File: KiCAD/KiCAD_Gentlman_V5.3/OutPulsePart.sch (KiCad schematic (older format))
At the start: 0 parts

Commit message: KSG : V5.3 회로도 초본 완성(검토 필요) 일부 부품 데이터시트 추가
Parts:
- added C17, C19, C24, C25, C26, C27, C28, C29, C31, C32, C36, C37, C39, C40: CAP_101K_250V_2012, symbol Custom:CAP_101K_250V_2012
- added C18, C30, C41, C46: CAP_220uF_6.3V_SC6.3X5.8, symbol Custom:CAP_220uF_6.3V_SC6.3X5.8
- added C20, C33, C42, C47: CAP_103K_250V_3216, symbol Custom:CAP_103K_250V_3216
- added C21, C22, C34, C35, C43, C44, C48, C49: CAP_105K_250V_4532, symbol Custom:CAP_105K_250V_4532
- added C23, C38, C45, C50, C?: CAP_103K_25V_1608, symbol Custom:CAP_103K_25V_1608
- added CN5: 12505WS-09(STRAIGHT), symbol Custom:Conn_01x09
- added CN6: 12505WS-08(STRAIGHT), symbol Custom:Conn_01x08
- added D11, D8, D9, D?: MBRAF3200T3G, Diode_SMD:D_SMA, symbol Custom:MBRAF3200T3G
- added FET1, FET2, FET3, FET4: FDT86246L, symbol Custom:FDT86246L
- added L1, L2, L3, L4: SC7850D-221K, symbol Custom:SC7850D-221K
- added Q10, Q11, Q12, Q15, Q16, Q17, Q18, Q23, Q24, Q25, Q26, Q27, Q28, Q29, Q30, Q9, Q? (x8): 2N5551S, symbol Custom:2N5551S
- added Q13, Q14, Q19, Q20, Q21, Q22, Q7, Q8, Q? (x4): 2N5401S, Package_TO_SOT_SMD:TSOT-23, symbol Custom:2N5401S
- added R100, R103, R106, R119, R120, R121, R122, R127, R130, R133, R136, R41, R42, R47, R50, R66, R67, R73, R76, R89, R90, R91, R92, R97, R?: R_1KF, symbol Custom:R_1KF
- added R101, R102, R104, R105, R107, R110, R111, R112, R113, R115, R116, R117, R118, R124, R126, R128, R129, R131, R132, R134, R135, R137, R32, R33, R39, R40, R44, R46, R48, R49, R51, R54, R55, R60, R70, R72, R74, R75, R77, R80, R81, R82, R83, R85, R86, R87, R88, R94, R96, R98, R99, R?: R_100KJ, symbol Custom:R_100KJ
- added R108, R114, R30, R38, R52, R59, R78, R84: R_150KF_2012, symbol Custom:R_150KF_2012
- added R109, R31, R53, R79: R_120RJ_3216, symbol Custom:R_120RJ_3216
- added R123, R43, R69, R93: R_100RJ, symbol Custom:R_100RJ
- added R125, R45, R71, R95: R_8.2KF, symbol Custom:R_8.2KF
- added R34, R35, R36, R37, R? (x8): R_2.7KF, symbol Custom:R_2.7KF
- added R?: R_0RJ_6432, symbol Custom:R_0RJ_6432
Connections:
- net labels added: +5V, CH1_OP1, CH1_OP2, CH1_P1_CTL1, CH1_P1_CTL2, CH1_P2_CTL1, CH1_P2_CTL2, CH2_OP1, CH2_OP2, CH2_P1_CTL1, CH2_P1_CTL2, CH2_P2_CTL1, CH2_P2_CTL2, CH3_OP1, CH3_OP2, CH3_OP3, CH3_OP4, CH3_P1_CTL1, CH3_P1_CTL2, CH3_P2_CTL1, CH3_P2_CTL2, CH3_P3_CTL1, CH3_P3_CTL2, CH3_P4_CTL1, CH3_P4_CTL2, CH4_OP1, CH4_OP2, CH4_OP3, CH4_OP4, CH4_P1_CTL1, CH4_P1_CTL2, CH4_P2_CTL1, CH4_P2_CTL2, CH4_P3_CTL1, CH4_P3_CTL2, CH4_P4_CTL1, CH4_P4_CTL2, CTL_CH1, CTL_CH2, CTL_CH3, CTL_CH4, GNDPWR, GNDREF, H_CURR_CH, H_VOLT_CH1, H_VOLT_CH2, H_VOLT_CH3, H_VOLT_CH4, N.C, RGB_B6, RGB_COM6, RGB_G6, RGB_R6
- wire segments 0 -> 533

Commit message: KSG : V5.3 회로도 완성, 심볼 정보 업데이트 완료(데이터시트 및 풋프린트 등), 기존 BOM과 일치 완료
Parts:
- C17, C19, C24, C25, C26, C27, C28, C29, C31, C32, C36, C37, C39, C40: footprint (none) -> Custom:C_0805_2012Metric; Comment (none) -> 101K/250V; Description (none) -> CHIP CERAMIC CAP; MAKER (none) -> WALSIN, SAMSUNG; TYPE (none) -> 2012
- C18, C30, C41, C46: footprint (none) -> Custom:C_Elec_6.3x5.8; Comment (none) -> 220uF/6.3V; Description (none) -> SMD ELECT CAPACITOR; Field4 (none) -> 220uF/6.3V; MAKER (none) -> SAMYOUNG; TYPE (none) -> SC 6.3X5.8; ValueView 220uF/6.3V -> (none)
- C20, C33, C42, C47: footprint (none) -> Custom:C_1206_3216Metric; Comment (none) -> TCC1206X7R103K251DT; Description (none) -> CHIP CERAMIC CAP; MAKER (none) -> CCTC; TYPE (none) -> 3216
- C21, C22, C34, C35, C43, C44, C48, C49: footprint (none) -> Custom:C_1812_4532Metric; Comment (none) -> FS43X105K251EGG; Description (none) -> CHIP CERAMIC CAP; MAKER (none) -> WALSIN; TYPE (none) -> 4532
- C23, C38, C45, C50: footprint (none) -> Custom:C_0603_1608Metric; Comment (none) -> 103K/25V; Description (none) -> CHIP CERAMIC CAP; MAKER (none) -> WALSIN, SAMSUNG; TYPE (none) -> 1608
- C51: renamed from C?; footprint (none) -> Custom:C_0603_1608Metric; Comment (none) -> 103K/25V; Description (none) -> CHIP CERAMIC CAP; MAKER (none) -> WALSIN, SAMSUNG; TYPE (none) -> 1608
- CN5: value 12505WS-09(STRAIGHT) -> 12505WS-09; footprint (none) -> Custom:12505WS-09; symbol Custom:Conn_01x09 -> Custom:12505WS-09; Comment (none) -> 12505WS-09; Description (none) -> SMD WAFER; MAKER (none) -> YEONHO ELECTRONICS; TYPE (none) -> SMD-9
- CN6: value 12505WS-08(STRAIGHT) -> 12505WS-08; footprint (none) -> Custom:12505WS-08; symbol Custom:Conn_01x08 -> Custom:12505WS-08; Comment (none) -> 12505WS-08; Description (none) -> SMD WAFER; MAKER (none) -> YEONHO ELECTRONICS; TYPE (none) -> SMD-8
- D10: renamed from D?; footprint Diode_SMD:D_SMA -> Custom:D_SMA; Comment (none) -> MBRAF3200T3G; Description (none) -> SMD DIODE SCHOTTKY; MAKER (none) -> MDD, ON SEMICONDUCTOR; TYPE (none) -> SMA
- D11, D8, D9: footprint Diode_SMD:D_SMA -> Custom:D_SMA; Comment (none) -> MBRAF3200T3G; Description (none) -> SMD DIODE SCHOTTKY; MAKER (none) -> MDD, ON SEMICONDUCTOR; TYPE (none) -> SMA
- FET1, FET2, FET3, FET4: footprint (none) -> Custom:SOT-223-3_TabPin2; Comment (none) -> FDT86246L; Description (none) -> SMD MOSFET N-CHANNEL; MAKER (none) -> FAIRCHILD; TYPE (none) -> SOT-223
- L1, L2, L3, L4: footprint (none) -> Custom:L_SC7850D-221K; Comment (none) -> SC7850D-221K; Description (none) -> SMD INDUCTOR; MAKER (none) -> SUHKWANG; TYPE (none) -> 7850
- Q10, Q11, Q12, Q15, Q16, Q17, Q18, Q23, Q24, Q25, Q26, Q27, Q28, Q29, Q30, Q9: footprint (none) -> Custom:SOT-23; Comment (none) -> 2N5551S; Description (none) -> CHIP TRANSISTOR; MAKER (none) -> FIRST SILICON; TYPE (none) -> SOT-23
- Q13, Q14, Q19, Q20, Q21, Q22, Q7, Q8: footprint Package_TO_SOT_SMD:TSOT-23 -> Custom:SOT-23; Comment (none) -> 2N5401S; Description (none) -> CHIP TRANSISTOR; MAKER (none) -> FIRST SILICON; TYPE (none) -> SOT-23
- Q31, Q32, Q33, Q34: renamed from Q?; footprint Package_TO_SOT_SMD:TSOT-23 -> Custom:SOT-23; Comment (none) -> 2N5401S; Description (none) -> CHIP TRANSISTOR; MAKER (none) -> FIRST SILICON; TYPE (none) -> SOT-23
- Q35, Q36, Q37, Q38, Q39, Q40, Q41, Q42: renamed from Q?; footprint (none) -> Custom:SOT-23; Comment (none) -> 2N5551S; Description (none) -> CHIP TRANSISTOR; MAKER (none) -> FIRST SILICON; TYPE (none) -> SOT-23
- R100, R103, R106, R119, R120, R121, R122, R127, R130, R133, R136, R41, R42, R47, R50, R66, R67, R73, R76, R89, R90, R91, R92, R97: footprint (none) -> Custom:R_0603_1608Metric; Comment (none) -> 1KF; Description (none) -> CHIP RESISTOR; MAKER (none) -> WALSIN, SAMSUNG; TYPE (none) -> 1608
- R101, R102, R104, R105, R107, R110, R111, R112, R113, R115, R116, R117, R118, R124, R126, R128, R129, R131, R132, R134, R135, R137, R32, R33, R39, R40, R44, R46, R48, R49, R51, R54, R55, R60, R70, R72, R74, R75, R77, R80, R81, R82, R83, R85, R86, R87, R88, R94, R96, R98, R99: footprint (none) -> Custom:R_0603_1608Metric; Comment (none) -> 100KJ; Description (none) -> CHIP RESISTOR; MAKER (none) -> WALSIN, SAMSUNG; TYPE (none) -> 1608
- R108, R114, R30, R38, R52, R59, R78, R84: footprint (none) -> Custom:R_0805_2012Metric; Comment (none) -> 150KF; Description (none) -> CHIP RESISTOR; MAKER (none) -> WALSIN, SAMSUNG; TYPE (none) -> 2012
- R109, R31, R53, R79: footprint (none) -> Custom:R_1206_3216Metric; Comment (none) -> 120RJ; Description (none) -> CHIP RESISTOR; MAKER (none) -> WALSIN, SAMSUNG; TYPE (none) -> 3216
- R123, R43, R69, R93: footprint (none) -> Custom:R_0603_1608Metric; Comment (none) -> 100RJ; Description (none) -> CHIP RESISTOR; MAKER (none) -> WALSIN, SAMSUNG; TYPE (none) -> 1608
- R125, R45, R71, R95: footprint (none) -> Custom:R_0603_1608Metric; Comment (none) -> 8.2KF; Description (none) -> CHIP RESISTOR; MAKER (none) -> WALSIN, SAMSUNG; TYPE (none) -> 1608
- R138: renamed from R?; footprint (none) -> Custom:R_3522_6432Metric; Comment (none) -> 0RJ; Description (none) -> CHIP RESISTOR; MAKER (none) -> WALSIN, SAMSUNG; TYPE (none) -> 6432
- R139: renamed from R?; footprint (none) -> Custom:R_0603_1608Metric; Comment (none) -> 1KF; Description (none) -> CHIP RESISTOR; MAKER (none) -> WALSIN, SAMSUNG; TYPE (none) -> 1608
- R34, R35, R36, R37: footprint (none) -> Custom:R_0603_1608Metric; Comment (none) -> 2.7KF; Description (none) -> CHIP RESISTOR; MAKER (none) -> WALSIN, SAMSUNG; TYPE (none) -> 1608
- R56, R57, R58, R62, R63, R64, R65, R68: renamed from R?; footprint (none) -> Custom:R_0603_1608Metric; Comment (none) -> 2.7KF; Description (none) -> CHIP RESISTOR; MAKER (none) -> WALSIN, SAMSUNG; TYPE (none) -> 1608
- R61: renamed from R?; footprint (none) -> Custom:R_0603_1608Metric; Comment (none) -> 100KJ; Description (none) -> CHIP RESISTOR; Field4 61 -> 100KJ; MAKER (none) -> WALSIN, SAMSUNG; TYPE (none) -> 1608

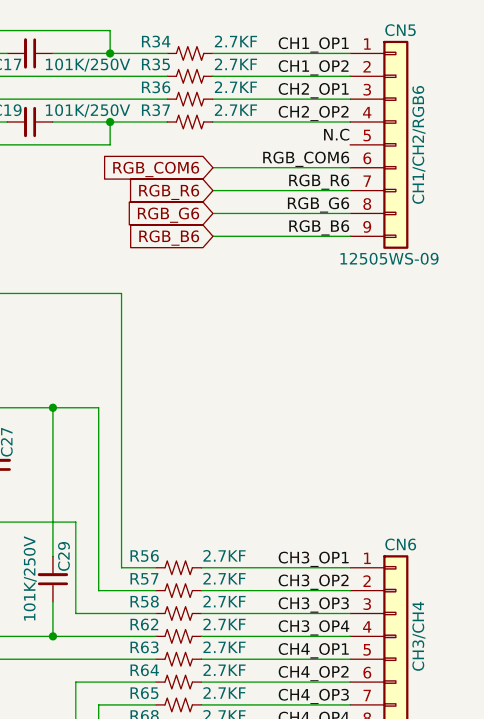
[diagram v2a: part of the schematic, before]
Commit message: KSG : 블루투스 회로도 작성 완료 (풋프린트 및 데이터시트 업데이트 완료)
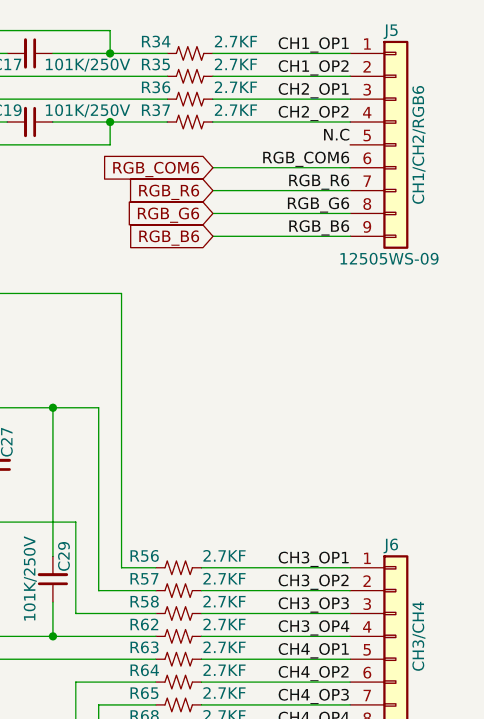
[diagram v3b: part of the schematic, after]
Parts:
- renumbered CN5 to J5, CN6 to J6
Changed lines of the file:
@@
 $Descr A3 16535 11693
 encoding utf-8
-Sheet 3 3
+Sheet 3 4
 Title "GentlemanV5.3"
 Date "2021-10-19"
@@
 Connection ~ 3350 7200
 $Comp
-L Custom:12505WS-09 CN5
+L Custom:12505WS-09 J5
 U 1 1 61F33BCC
 P 15450 1200
-F 0 "CN5" H 15400 1700 50  0000 L CNN
+F 0 "J5" H 15400 1700 50  0000 L CNN
 F 1 "12505WS-09" H 15200 700 50  0000 L CNN
 F 2 "Custom:12505WS-09" H 15450 1200 50  0001 C CNN
@@
 $EndComp
 $Comp
-L Custom:12505WS-08 CN6
+L Custom:12505WS-08 J6
 U 1 1 61F314D1
 P 15450 3350
-F 0 "CN6" H 15400 3750 50  0000 L CNN
+F 0 "J6" H 15400 3750 50  0000 L CNN
 F 1 "12505WS-08" H 15200 2850 50  0000 L CNN
 F 2 "Custom:12505WS-08" H 15450 3350 50  0001 C CNN

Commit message: KSG : V5.3B용으로 회로도 수정 및 PCB 아트웤 완료.(샘플PCB주문됨)
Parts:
- C17, C19, C24, C25, C26, C27, C28, C29, C31, C32, C36, C37, C39, C40: Comment 101K/250V -> (none); Description CHIP CERAMIC CAP -> (none); Field4 101K/250V -> (none); MAKER WALSIN, SAMSUNG -> (none); Maker (none) -> WALSIN, SAMSUNG; PartName (none) -> 101K/250V; Replacement (none) -> CC0805JRNPOYBN101; Shop (none) -> https://www.eleparts.co.kr/goods/view?no=9594793; TYPE 2012 -> (none); Type (none) -> CHIP CERAMIC CAP
- C18, C30, C41, C46: Comment 220uF/6.3V -> (none); Description SMD ELECT CAPACITOR -> (none); Field4 220uF/6.3V -> (none); Field5 SC 6.3X5.8 -> (none); MAKER SAMYOUNG -> (none); Maker (none) -> SAMYOUNG; PartName (none) -> 220uF/6.3V; Shop (none) -> https://www.eleparts.co.kr/goods/view?no=3369557; TYPE SC 6.3X5.8 -> (none); Type (none) -> SMD ELECT CAPACITOR
- C20, C33, C42, C47: Comment TCC1206X7R103K251DT -> (none); Description CHIP CERAMIC CAP -> (none); Field4 TCC1206X7R103K251DT -> (none); MAKER CCTC -> (none); Maker (none) -> CCTC; PartName (none) -> TCC1206X7R103K251DT; Shop (none) -> https://www.eleparts.co.kr/goods/view?no=8016042; TYPE 3216 -> (none); Type (none) -> CHIP CERAMIC CAP
- C21, C22, C34, C35, C43, C44, C48, C49: Comment FS43X105K251EGG -> (none); Description CHIP CERAMIC CAP -> (none); Field4 FS43X105K251EGG -> (none); MAKER WALSIN -> (none); Maker (none) -> WALSIN; PartName (none) -> FS43X105K251EGG; Shop (none) -> https://www.eleparts.co.kr/goods/view?no=8016951; TYPE 4532 -> (none); Type (none) -> CHIP CERAMIC CAP
- C23, C38, C45, C50, C51: Comment 103K/25V -> (none); Description CHIP CERAMIC CAP -> (none); Field4 103K/25V -> (none); MAKER WALSIN, SAMSUNG -> (none); Maker (none) -> WALSIN, SAMSUNG; PartName (none) -> 103K/25V; Replacement (none) -> CC0603KRX7R8BB103; Shop (none) -> https://www.eleparts.co.kr/goods/view?no=8057789#goodConten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; TYPE 1608 -> (none); Type (none) -> CHIP CERAMIC CAP
- D10, D11, D8, D9: Comment MBRAF3200T3G -> (none); Description SMD DIODE SCHOTTKY -> (none); MAKER MDD, ON SEMICONDUCTOR -> (none); Maker (none) -> MDD, ON SEMICONDUCTOR; PartName (none) -> MBRAF3200T3G; Replacement (none) -> SS1200-LTP; Shop (none) -> https://www.eleparts.co.kr/goods/view?no=1799117; TYPE SMA -> (none); Type (none) -> SMD DIODE SCHOTTKY
- FET1, FET2, FET3, FET4: Comment FDT86246L -> (none); Description SMD MOSFET N-CHANNEL -> (none); MAKER FAIRCHILD -> (none); Maker (none) -> FAIRCHILD; PartName (none) -> FDT86246L; Shop (none) -> https://www.eleparts.co.kr/goods/view?no=6008399; TYPE SOT-223 -> (none); Type (none) -> SMD MOSFET N-CHANNEL
- J5: Comment 12505WS-09 -> (none); Description SMD WAFER -> (none); Field4 CH1/CH2/RGB6 -> (none); MAKER YEONHO ELECTRONICS -> (none); Maker (none) -> YEONHO ELECTRONICS; PartName (none) -> 12505WS-09; Shop (none) -> https://www.devicemart.co.kr/goods/view?no=12012614; TYPE SMD-9 -> (none); Type (none) -> SMD WAFER
- J6: Comment 12505WS-08 -> (none); Description SMD WAFER -> (none); Field4 CH3/CH4 -> (none); MAKER YEONHO ELECTRONICS -> (none); Maker (none) -> YEONHO ELECTRONICS; PartName (none) -> 12505WS-08; Shop (none) -> https://www.devicemart.co.kr/goods/view?no=12012611; TYPE SMD-8 -> (none); Type (none) -> SMD WAFER
- L1, L2, L3, L4: Comment SC7850D-221K -> (none); Description SMD INDUCTOR -> (none); MAKER SUHKWANG -> (none); Maker (none) -> SUHKWANG; PartName (none) -> SC7850D-221K; Shop (none) -> https://www.devicemart.co.kr/goods/view?no=6606; TYPE 7850 -> (none); Type (none) -> SMD INDUCTOR
- Q10, Q11, Q12, Q15, Q16, Q17, Q18, Q23, Q24, Q25, Q26, Q27, Q28, Q29, Q30, Q35, Q36, Q37, Q38, Q39, Q40, Q41, Q42, Q9: Comment 2N5551S -> (none); Description CHIP TRANSISTOR -> (none); MAKER FIRST SILICON -> (none); Maker (none) -> FIRST SILICON; PartName (none) -> 2N5551S; Replacement (none) -> 2N5551S-RTK/P; Shop (none) -> KEC Semicon; TYPE SOT-23 -> (none); Type (none) -> CHIP TRANSISTOR
- Q13, Q14, Q19, Q20, Q21, Q22, Q31, Q32, Q33, Q34, Q7, Q8: Comment 2N5401S -> (none); Description CHIP TRANSISTOR -> (none); MAKER FIRST SILICON -> (none); Maker (none) -> FIRST SILICON; PartName (none) -> 2N5401S; Replacement (none) -> 2N5401S-RTK/P; Shop (none) -> https://www.eleparts.co.kr/goods/view?no=6561296; TYPE SOT-23 -> (none); Type (none) -> CHIP TRANSISTOR
- R100, R103, R106, R119, R120, R121, R122, R127, R130, R133, R136, R139, R41, R42, R47, R50, R66, R67, R73, R76, R89, R90, R91, R92, R97: Comment 1KF -> (none); Description CHIP RESISTOR -> (none); Field4 1KF -> (none); MAKER WALSIN, SAMSUNG -> (none); Maker (none) -> WALSIN, SAMSUNG; PartName (none) -> 1KF; TYPE 1608 -> (none); Type (none) -> CHIP RESISTOR
- R101, R102, R104, R105, R107, R110, R111, R112, R113, R115, R116, R117, R118, R124, R126, R128, R129, R131, R132, R134, R135, R137, R32, R33, R39, R40, R44, R46, R48, R49, R51, R54, R55, R60, R61, R70, R72, R74, R75, R77, R80, R81, R82, R83, R85, R86, R87, R88, R94, R96, R98, R99: Comment 100KJ -> (none); Description CHIP RESISTOR -> (none); Field4 100KJ -> (none); MAKER WALSIN, SAMSUNG -> (none); Maker (none) -> WALSIN, SAMSUNG; PartName (none) -> 100KJ; TYPE 1608 -> (none); Type (none) -> CHIP RESISTOR
- R108, R114, R30, R38, R52, R59, R78, R84: Comment 150KF -> (none); Description CHIP RESISTOR -> (none); Field4 150KF -> (none); MAKER WALSIN, SAMSUNG -> (none); Maker (none) -> WALSIN, SAMSUNG; PartName (none) -> 150KF; TYPE 2012 -> (none); Type (none) -> CHIP RESISTOR
- R109, R31, R53, R79: Comment 120RJ -> (none); Description CHIP RESISTOR -> (none); Field4 120RJ -> (none); MAKER WALSIN, SAMSUNG -> (none); Maker (none) -> WALSIN, SAMSUNG; PartName (none) -> 120RJ; TYPE 3216 -> (none); Type (none) -> CHIP RESISTOR
- R123, R43, R69, R93: Comment 100RJ -> (none); Description CHIP RESISTOR -> (none); Field4 100RJ -> (none); MAKER WALSIN, SAMSUNG -> (none); Maker (none) -> WALSIN, SAMSUNG; PartName (none) -> 100RJ; TYPE 1608 -> (none); Type (none) -> CHIP RESISTOR
- R125, R45, R71, R95: Comment 8.2KF -> (none); Description CHIP RESISTOR -> (none); Field4 8.2KF -> (none); MAKER WALSIN, SAMSUNG -> (none); Maker (none) -> WALSIN, SAMSUNG; PartName (none) -> 8.2KF; TYPE 1608 -> (none); Type (none) -> CHIP RESISTOR
- R138: Comment 0RJ -> (none); Description CHIP RESISTOR -> (none); Field4 0RJ -> (none); MAKER WALSIN, SAMSUNG -> (none); Maker (none) -> WALSIN, SAMSUNG; PartName (none) -> 0RJ; TYPE 6432 -> (none); Type (none) -> CHIP RESISTOR
- R34, R35, R36, R37, R56, R57, R58, R62, R63, R64, R65, R68: Comment 2.7KF -> (none); Description CHIP RESISTOR -> (none); Field4 2.7KF -> (none); MAKER WALSIN, SAMSUNG -> (none); Maker (none) -> WALSIN, SAMSUNG; PartName (none) -> 2.7KF; TYPE 1608 -> (none); Type (none) -> CHIP RESISTOR
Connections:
- net CH1_OP1: no longer C24.1, C24.2, C25.1, C25.2, C26.1, C26.2, C27.1, C27.2, C28.1, C28.2, C29.1, C29.2, C31.1, C31.2, C32.1, C32.2, C36.1, C36.2, C37.1, C37.2, C39.1, C39.2, C40.1, C40.2, J5.1 (Pin_1), R34.1, R56.2, R57.2, R58.2, R62.2, R63.2, R64.2, R65.2, R68.2
- net CH1_OP2: no longer J5.2 (Pin_2), R35.1
- net CH2_OP1: no longer J5.3 (Pin_3), R36.1
- net CH2_OP2: no longer J5.4 (Pin_4), R37.1
- net CH3_OP1: now also C24.2, C25.2, C27.2, R56.2; no longer J6.1 (Pin_1), R56.1
- net CH3_OP2: now also C24.1, C26.2, C29.2, R57.2; no longer J6.2 (Pin_2), R57.1
- net CH3_OP3: now also C25.1, C26.1, C28.2, R58.2; no longer J6.3 (Pin_3), R58.1
- net CH3_OP4: now also C27.1, C28.1, C29.1, R62.2; no longer J6.4 (Pin_4), R62.1
- net CH4_OP1: now also C31.2, C32.2, C37.2, R63.2; no longer J6.5 (Pin_5), R63.1
- net CH4_OP2: now also C31.1, C36.2, C40.2, R64.2; no longer J6.6 (Pin_6), R64.1
- net CH4_OP3: now also C32.1, C36.1, C39.2, R65.2; no longer J6.7 (Pin_7), R65.1
- net CH4_OP4: now also C37.1, C39.1, C40.1, R68.2; no longer J6.8 (Pin_8), R68.1
- net N.C: no longer names the net of J5.5 (Pin_5)
- new net: J6.1 (Pin_1), R56.1
- new net: J6.2 (Pin_2), R57.1
- new net: J6.3 (Pin_3), R58.1
- new net: J6.4 (Pin_4), R62.1
- new net: J6.5 (Pin_5), R63.1
- new net: J6.6 (Pin_6), R64.1
- new net: J6.7 (Pin_7), R65.1
- new net: J6.8 (Pin_8), R68.1
- new net: J5.1 (Pin_1), R34.1
- new net: J5.2 (Pin_2), R35.1
- new net: J5.3 (Pin_3), R36.1
- new net: J5.4 (Pin_4), R37.1
- no-connect marks 0 -> 1
